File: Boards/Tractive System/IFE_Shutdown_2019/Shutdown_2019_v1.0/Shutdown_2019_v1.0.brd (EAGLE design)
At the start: 88.9 x 76.2 mm, 108 parts, among them Q1 DMN6140L-7, Q11 DMP3099L-7, Q12 IRLML6346PBF, Q13 IRLML6346PBF, Q14 IRLML6346PBF, Q15 DMP3099L-7, Q16 DMN6140L-7, Q17 IRLML6346PBF, Q2 DMN6140L-7, Q3 DMN6140L-7, Q4 DMN6140L-7, Q5 DMN6140L-7, Q6 DMP3099L-7, Q7 DMN6140L-7, Q8 DMN6140L-7, Q9 DMN6140L-7, U1 STM32F103CBT6

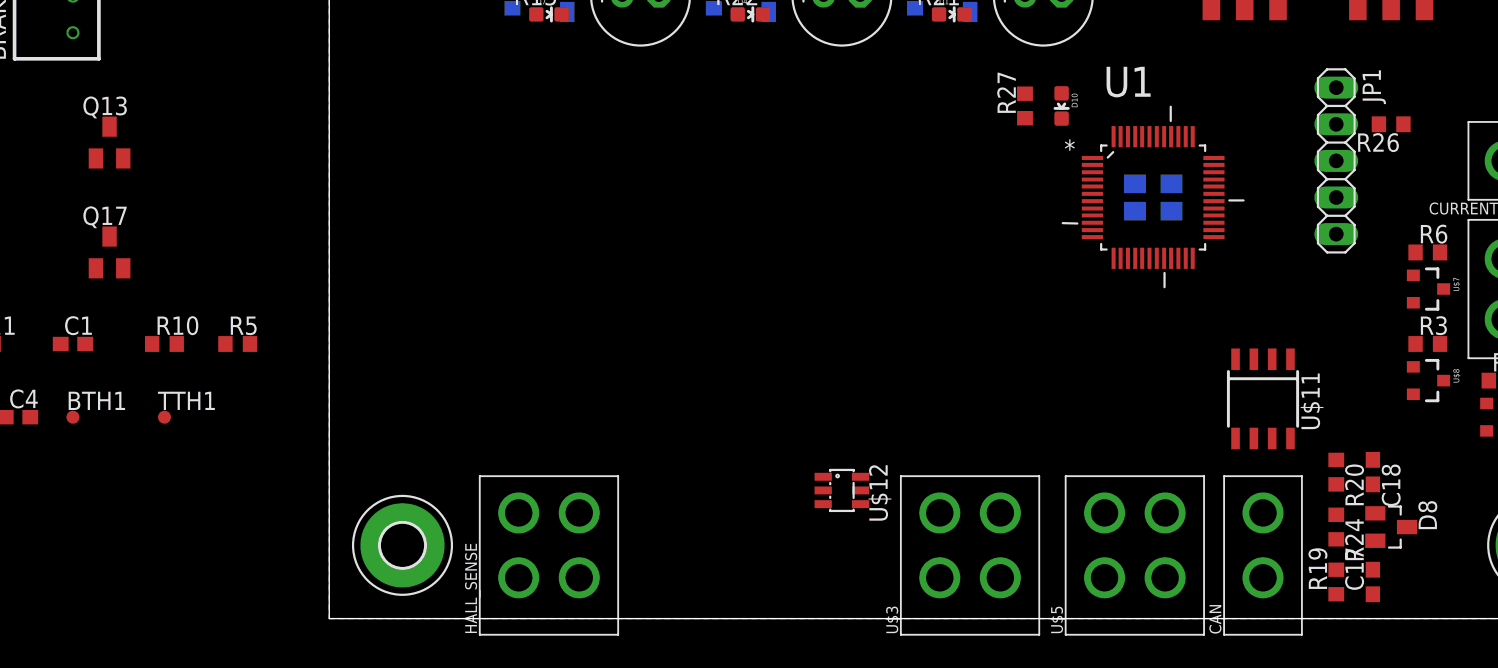
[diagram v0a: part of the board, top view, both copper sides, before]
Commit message: Added traction control mucrocontroller
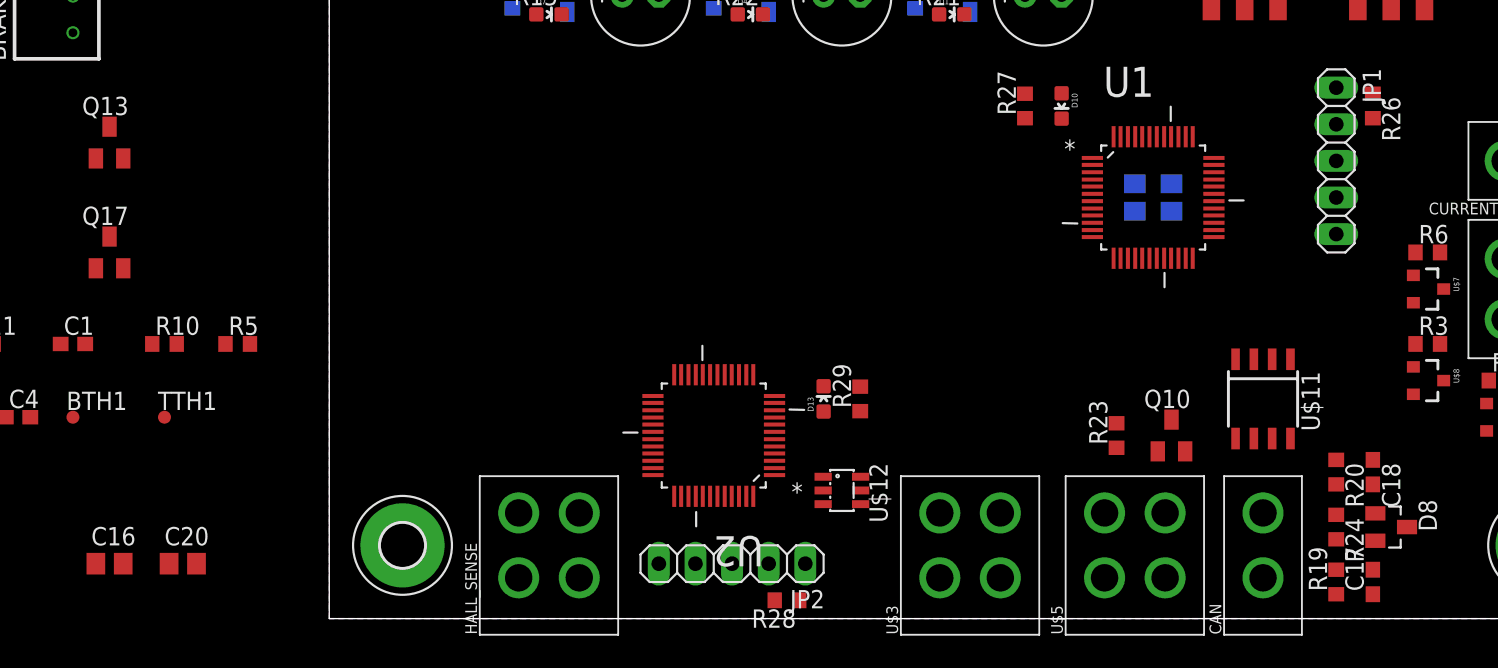
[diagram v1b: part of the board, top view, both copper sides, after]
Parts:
- added C16, C20: 1u, rcl:C0805
- added D13: RED, SparkFun-LED:LED-0603
- added JP2: (no value), Headers_IFE:1X05
- added Q10: DMN6140L-7, TRANS:SOT23
- added R23: 10k, resistor:R0603
- added R28, R29: 10k, rcl:R0603
- added U2: STM32F103CBT6, ST Microelctronics_By_element14_Batch_1:QFP50P900X900X160-48N
- R9: value (none) -> 1k
- moved R26 1.80 mm to (72.4, 35.6), turned to 270 degrees
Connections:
- new net !RST_TC: JP2.2, R28.2, U2.7
- new net BRAKE_PRESSURE_3_3: U1.19
- new net DEBUG_TC: D13.C, U2.2
- new net HV_CONNECTED_3_3: Q10.3, R23.1, U1.21
- new net I2C1_SCL: U1.42
- new net I2C1_SDA: U1.43
- new net N$18: U1.30
- new net N$20: U1.27
- new net N$21: D13.A, R29.2
- new net N$22: U$12.4
- new net N$23: U$12.3
- new net N$5: U1.29
- new net REGEN_3_3: U1.10
- new net SCL_TC: U2.42
- new net SDA_TC: U2.43
- new net SWCLK_TC: JP2.4, U2.37
- new net SWDIO_TC: JP2.3, U2.34
- new net THROTTLE_3_3: U1.18
- net +3V3: now also C16.1, C20.1, JP2.1, R23.2, R28.1, R29.1, U2.24, U2.36, U2.48, U2.9
- net BRAKE_LIGHT_EN: now also U1.26
- net CAN_RX: now also U1.32; no longer U1.45
- net CAN_SBTY: now also U1.31; no longer U1.43
- net CAN_TX: now also U1.33; no longer U1.46
- net GND: now also C16.2, C20.2, JP2.5, Q10.2, U2.20, U2.23, U2.35, U2.44, U2.47, U2.8
- net HV_CONNECTED: now also Q10.1
- net PA11: now also U2.32; no longer U1.32
- net SPI1_MISO: now also U2.17
- net SPI1_MOSI: now also U2.16
- net SPI1_NSS: now also U2.14
- net SPI1_SCK: now also U2.15
- net TSAL_HV_EN: now also U1.22
- net TSAL_LV_EN: now also U1.25

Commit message: Rework Enable
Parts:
- removed D3, D5, D6: 1N914, Diodes:SOD323-F
- removed Q4, Q7, Q8: DMN6140L-7, TRANS:SOT23
- removed R2, R4, R7: 10k, rcl:R0603
- removed R_APPS, R_BTSF, R_RTD: PCN-112D3MHZ, Display_Custom:TH_SPST_PCN_D3M_TE_CONN
- removed R_BMS, R_BSPD, R_IMD: RT424012, Display_Custom:TH_DPDT_GEN_PURPOSE_2.54
- added Q18, Q20, Q21: DMN6140L-7, TRANS:SOT23
- added R30, R31, R32: 10k, rcl:R0603
- added U$13, U$14, U$15: EC2, KEMET:DPDT_2.54
- C2, C8, C9: value 47u -> 10uF; device rcl:E2,5-7 -> rcl:C0805
- moved C2 2.54 mm to (19.1, 43.2), turned to 270 degrees
- moved C8 2.54 mm to (33.0, 43.2), turned to 270 degrees
- moved C9 2.54 mm to (47.0, 43.2), turned to 270 degrees
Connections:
- net THROTTLE_3_3 renamed THROTTLE_A_3_3
- removed net N$10: D5.A, Q7.3, R_BTSF.2
- removed net N$11: D6.A, Q8.3, R_RTD.2
- removed net N$12: R_BTSF.3, R_RTD.4
- removed net N$13: R_APPS.3, R_BTSF.4
- removed net N$20: U1.27
- removed net N$7: D3.A, Q4.3, R_APPS.2
- new net HALL_FL_3_3: U2.25
- new net HALL_FR_3_3: U2.26
- new net HALL_RL_3_3: U2.27
- new net HALL_RR_3_3: U2.28
- new net N$24: Q18.3, Q20.2
- new net N$25: Q18.2, Q21.3
- new net RTDS_EN: U1.39
- new net THROTTLE_B_3_3: U1.19
- net +12V: now also U$13.$P5, U$14.$P5, U$15.$P5; no longer D3.C, D5.C, D6.C, R_APPS.1, R_BMS.24, R_BSPD.24, R_BTSF.1, R_IMD.24, R_RTD.1
- net AIR_IN: now also U$13.$P9; no longer R_BSPD.11
- net AIR_OUT: now also U$15.$P8; no longer R_IMD.14
- net APPS_EN: now also Q20.1, R30.2, U1.40; no longer Q4.1, R2.2
- net BRAKE_PRESSURE_3_3: now also U1.10; no longer U1.19
- net BTSF_EN: now also Q18.1, R31.2, U1.41; no longer Q7.1, R4.2
- net ENABLE_IN: now also Q21.2; no longer R_APPS.4
- net ENABLE_OUT: now also Q20.3; no longer R_RTD.3
- net FAULT_BMS_STAT: now also C8.1, U$14.$P1, U$14.$P4; no longer C8.+, R_BMS.21, R_BMS.A1
- net FAULT_BSPD_STAT: now also C2.1, U$13.$P1, U$13.$P4; no longer C2.+, R_BSPD.21, R_BSPD.A1
- net FAULT_BSPD_STATUS_3_3: now also U1.27; no longer U1.11
- net FAULT_IMD_STAT: now also C9.1, U$15.$P1, U$15.$P4; no longer C9.+, R_IMD.21, R_IMD.A1
- net GND: now also C2.2, C8.2, C9.2, R30.1, R31.1, R32.1; no longer C2.-, C8.-, C9.-, Q4.2, Q7.2, Q8.2, R2.1, R4.1, R7.1
- net N$1: now also U$14.$P12; no longer R_BMS.A2
- net N$27: now also U$13.$P8, U$14.$P9; no longer R_BMS.11, R_BSPD.14
- net N$28: now also U$13.$P3; no longer R_BSPD.22
- net N$31: now also U$14.$P8, U$15.$P9; no longer R_BMS.14, R_IMD.11
- net N$32: now also U$13.$P12; no longer R_BSPD.A2
- net N$35: now also U$14.$P3; no longer R_BMS.22
- net N$43: now also U$15.$P3; no longer R_IMD.22
- net N$44: now also U$15.$P12; no longer R_IMD.A2
- net REGEN_3_3: now also U1.11; no longer U1.10
- net RTD_EN: now also Q21.1, R32.2, U1.45; no longer Q8.1, R7.2

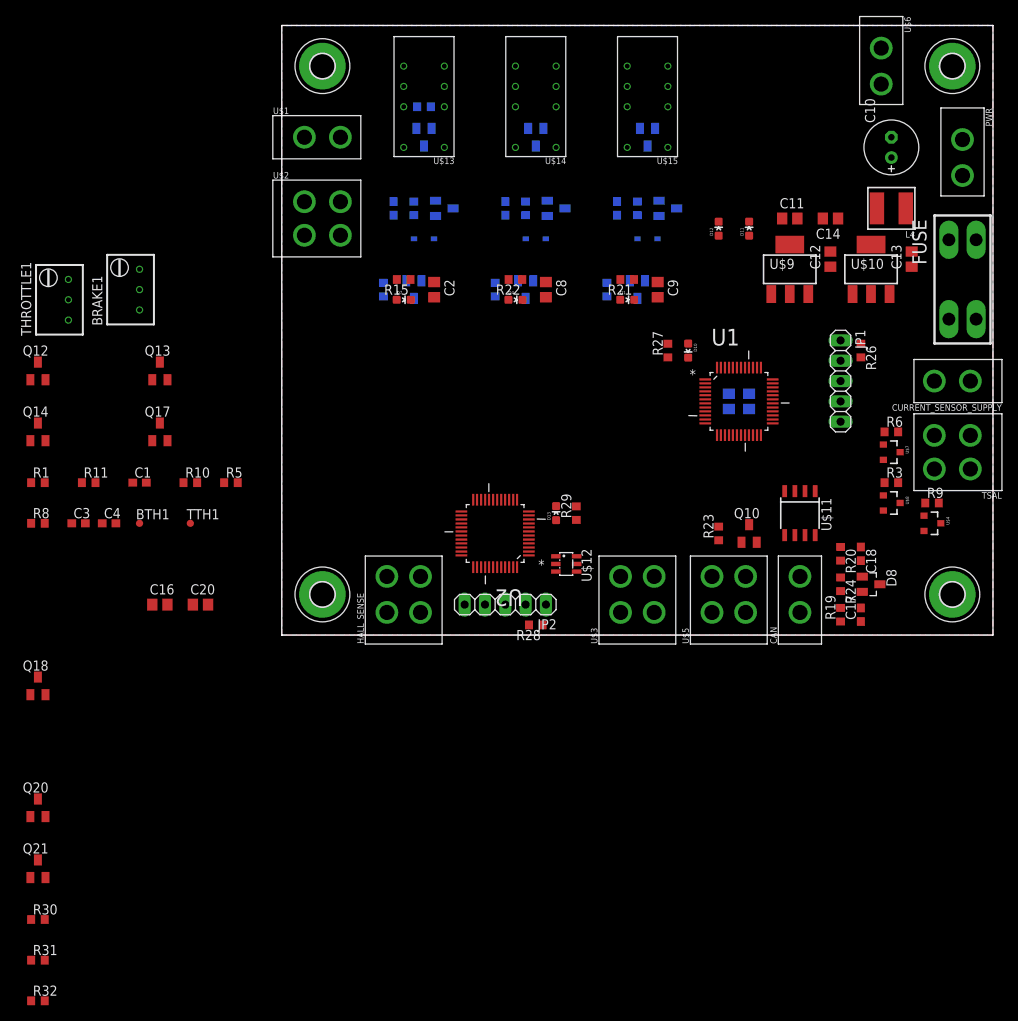
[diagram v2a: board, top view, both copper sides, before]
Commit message: created op amp buffer
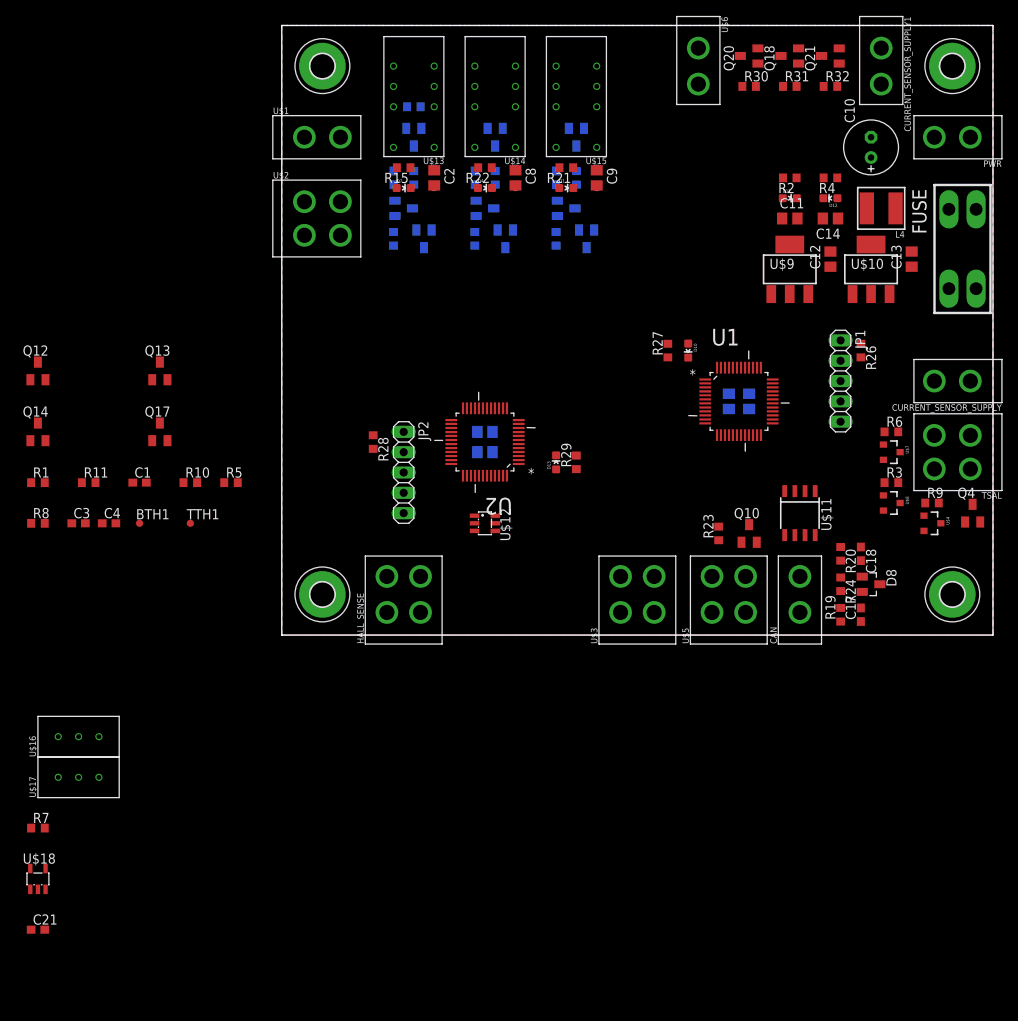
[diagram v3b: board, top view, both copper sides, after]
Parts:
- removed BRAKE1, THROTTLE1: RTRIM3249W, Resistors:RTRIM3299W
- added C21: (no value), rcl:C0603
- added CURRENT_SENSOR_SUPPLY1: MINIFIT_JR_5566-02, Display_Custom:MINIFIT_JR_5566-02
- added Q4: DMN6140L-7, TRANS:SOT23
- added R2, R4: (no value), rcl:R0603
- added R7: 50k, rcl:R0603
- added U$16, U$17: PV36, BOURNS:PV36
- added U$18: LMV321L, STM:SOT23-5
- moved R32 151.3 mm to (68.6, 68.6)
- moved R31 144.1 mm to (63.5, 68.6)
- moved Q21 141.9 mm to (68.6, 72.4), turned to 90 degrees
- moved R30 136.9 mm to (58.4, 68.6)
- moved Q20 129.4 mm to (58.4, 72.4), turned to 90 degrees
- moved Q18 122.6 mm to (63.5, 72.4), turned to 90 degrees
- moved C16 46.0 mm to (25.4, 25.4), flipped to the bottom
- moved C20 40.3 mm to (25.4, 22.9), flipped to the bottom, turned to 180 degrees
- moved R28 30.6 mm to (11.4, 24.1), turned to 270 degrees
- moved U$6 22.9 mm to (52.1, 71.1)
- moved JP2 20.8 mm to (15.2, 20.3), turned to 270 degrees
- moved D1 15.9 mm to (35.6, 55.9)
- moved C9 15.9 mm to (39.4, 57.1)
- moved R21 15.9 mm to (35.6, 58.4)
- moved D4 14.5 mm to (25.4, 55.9)
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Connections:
- removed net RESET: U$5.4
- new net N$10: D12.C, R4.2
- new net N$11: D11.C, R2.2
- new net N$12: R7.2, U$12.5, U$18.1
- new net N$20: U$12.6
- new net N$7: Q4.3
- net +3V3: now also D11.A
- net +5V: now also C21.1, CURRENT_SENSOR_SUPPLY1.1, D12.A, U$12.1, U$16.A, U$17.A, U$18.5; no longer BRAKE1.1, THROTTLE1.1
- net BRAKE_TH: now also U$16.W; no longer BRAKE1.2
- net FAULT_RESET: now also U$5.4
- net GND: now also C21.2, Q4.2, R2.1, R4.1, R7.1, U$12.2, U$16.B, U$17.B, U$18.2; no longer BRAKE1.3, THROTTLE1.3
- net HV_CONNECTED: now also CURRENT_SENSOR_SUPPLY1.2; no longer U$5.2
- net RTDS_EN: now also Q4.1
- net THROTTLE_OUT: now also U$18.3, U$18.4
- net THROTTLE_TH: now also U$17.W; no longer THROTTLE1.2
